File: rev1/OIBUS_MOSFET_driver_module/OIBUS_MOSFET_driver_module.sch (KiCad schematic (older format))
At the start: 149 parts, among them J1 SWD, J10 +, J11 +, J12 +, J13 +, J2 UART, J3 5V - 24V, Molex Ultrafit, J4 +, J5 +, J6 +, J7 +, J8 +, J9 +, T1 DMG6402LVT, T10 DMG6402LVT, T2 DMG6402LVT, T3 DMG6402LVT, T4 DMG6402LVT, T5 DMG6402LVT, T6 DMG6402LVT, T7 DMG6402LVT, T8 DMG6402LVT, T9 DMG6402LVT, U1 TLP291, U10 STM32F303CCTx, U11 TLP291, U12 TLP291, U2 TLP291, U3 TLP291, U4 TLP291, U5 TLP291, U6 TLP291, U7 TLP291, U8 TLP291, U9 TCAN330, Y1 16M

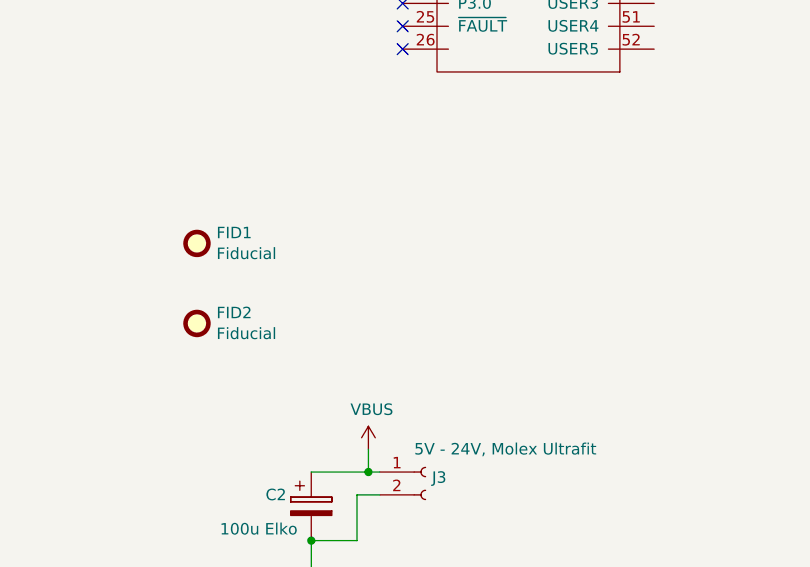
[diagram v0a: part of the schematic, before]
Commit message: disabling bottom solder stencil. uploading to aisler
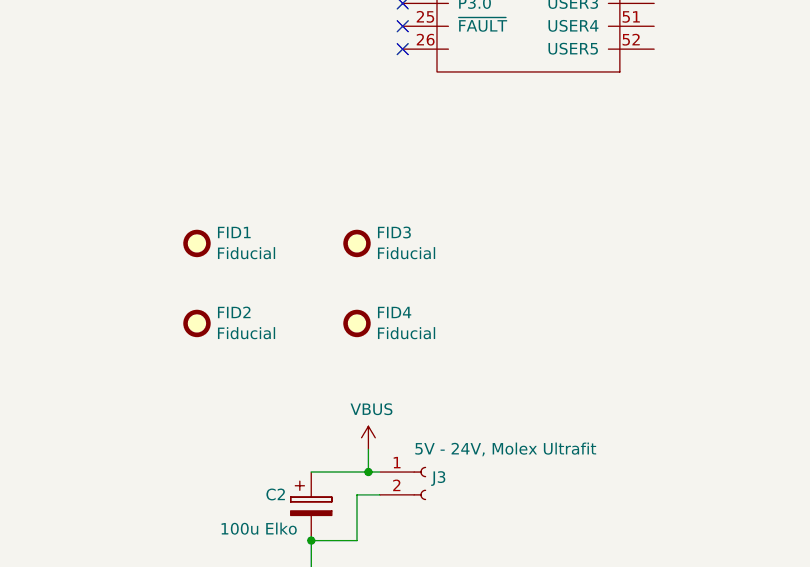
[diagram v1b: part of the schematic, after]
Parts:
- added FID3, FID4: Fiducial, Fiducials:Fiducial_1mm_Dia_2mm_Outer, symbol Mechanical:Fiducial
- FID1, FID2: footprint Fiducial:Fiducial_1mm_Dia_2mm_Outer -> Fiducials:Fiducial_1mm_Dia_2mm_Outer
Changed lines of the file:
@@
 F 0 "FID1" H 9685 9246 50  0000 L CNN
 F 1 "Fiducial" H 9685 9155 50  0000 L CNN
-F 2 "Fiducial:Fiducial_1mm_Dia_2mm_Outer" H 9600 9200 50  0001 C CNN
+F 2 "Fiducials:Fiducial_1mm_Dia_2mm_Outer" H 9600 9200 50  0001 C CNN
 F 3 "~" H 9600 9200 50  0001 C CNN
 	1    9600 9200
@@
 F 0 "FID2" H 9685 9596 50  0000 L CNN
 F 1 "Fiducial" H 9685 9505 50  0000 L CNN
-F 2 "Fiducial:Fiducial_1mm_Dia_2mm_Outer" H 9600 9550 50  0001 C CNN
+F 2 "Fiducials:Fiducial_1mm_Dia_2mm_Outer" H 9600 9550 50  0001 C CNN
 F 3 "~" H 9600 9550 50  0001 C CNN
 	1    9600 9550
@@
 Wire Wire Line
 	11650 7150 11650 7200
+$Comp
+L Mechanical:Fiducial FID4
+U 1 1 5C341F6F
+P 10300 9550
+F 0 "FID4" H 10385 9596 50  0000 L CNN
+F 1 "Fiducial" H 10385 9505 50  0000 L CNN
+F 2 "Fiducials:Fiducial_1mm_Dia_2mm_Outer" H 10300 9550 50  0001 C CNN
+F 3 "~" H 10300 9550 50  0001 C CNN
+	1    10300 9550
+	1    0    0    -1
+$EndComp
+$Comp
+L Mechanical:Fiducial FID3
+U 1 1 5C3420AA
+P 10300 9200
+F 0 "FID3" H 10385 9246 50  0000 L CNN
+F 1 "Fiducial" H 10385 9155 50  0000 L CNN
+F 2 "Fiducials:Fiducial_1mm_Dia_2mm_Outer" H 10300 9200 50  0001 C CNN
+F 3 "~" H 10300 9200 50  0001 C CNN
+	1    10300 9200
+	1    0    0    -1
+$EndComp
 $EndSCHEMATC

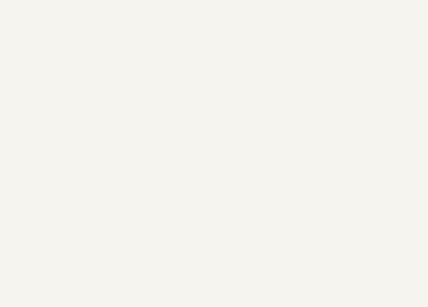
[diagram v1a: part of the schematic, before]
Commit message: silkscreen labels added
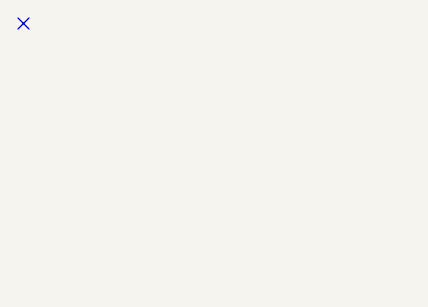
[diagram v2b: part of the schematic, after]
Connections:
- no-connect marks 75 -> 76
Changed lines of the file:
@@
 	1    0    0    -1
 $EndComp
+NoConn ~ -4300 -4150
 $EndSCHEMATC

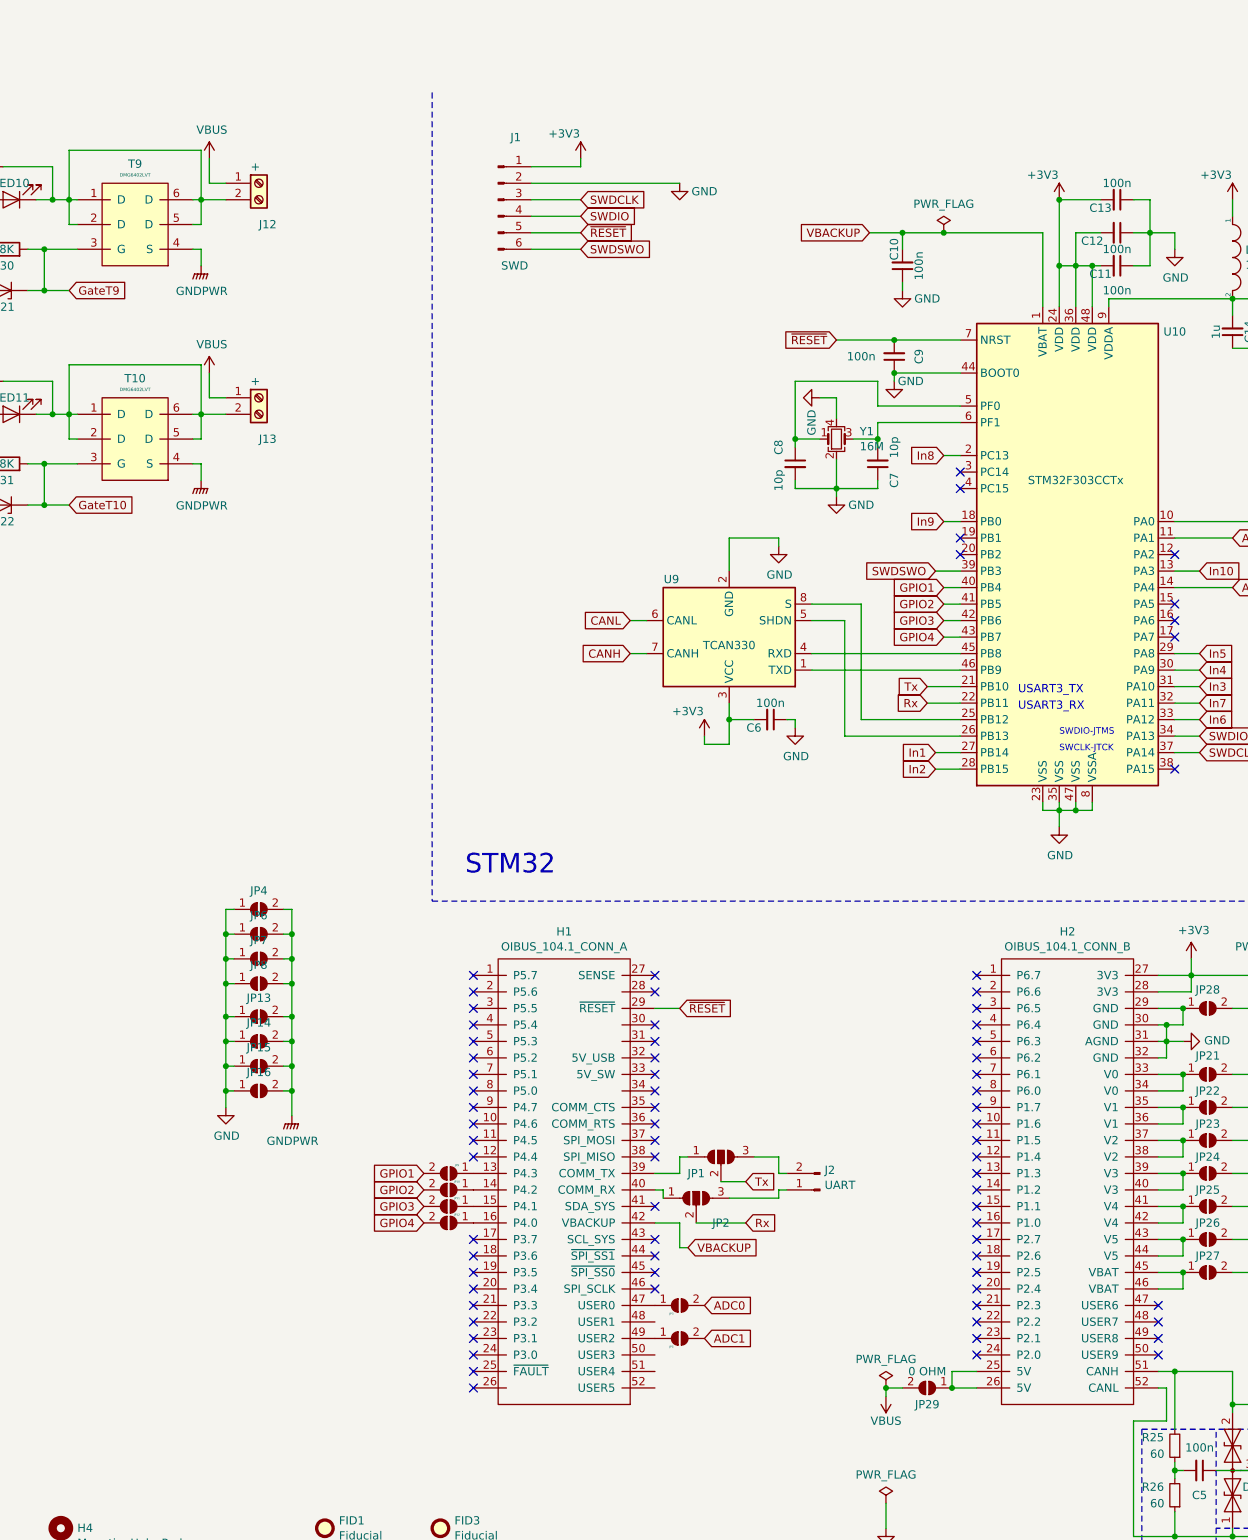
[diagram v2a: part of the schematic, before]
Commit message: fixing zener footprint, rotating leds for side view, added uavcan micro connector
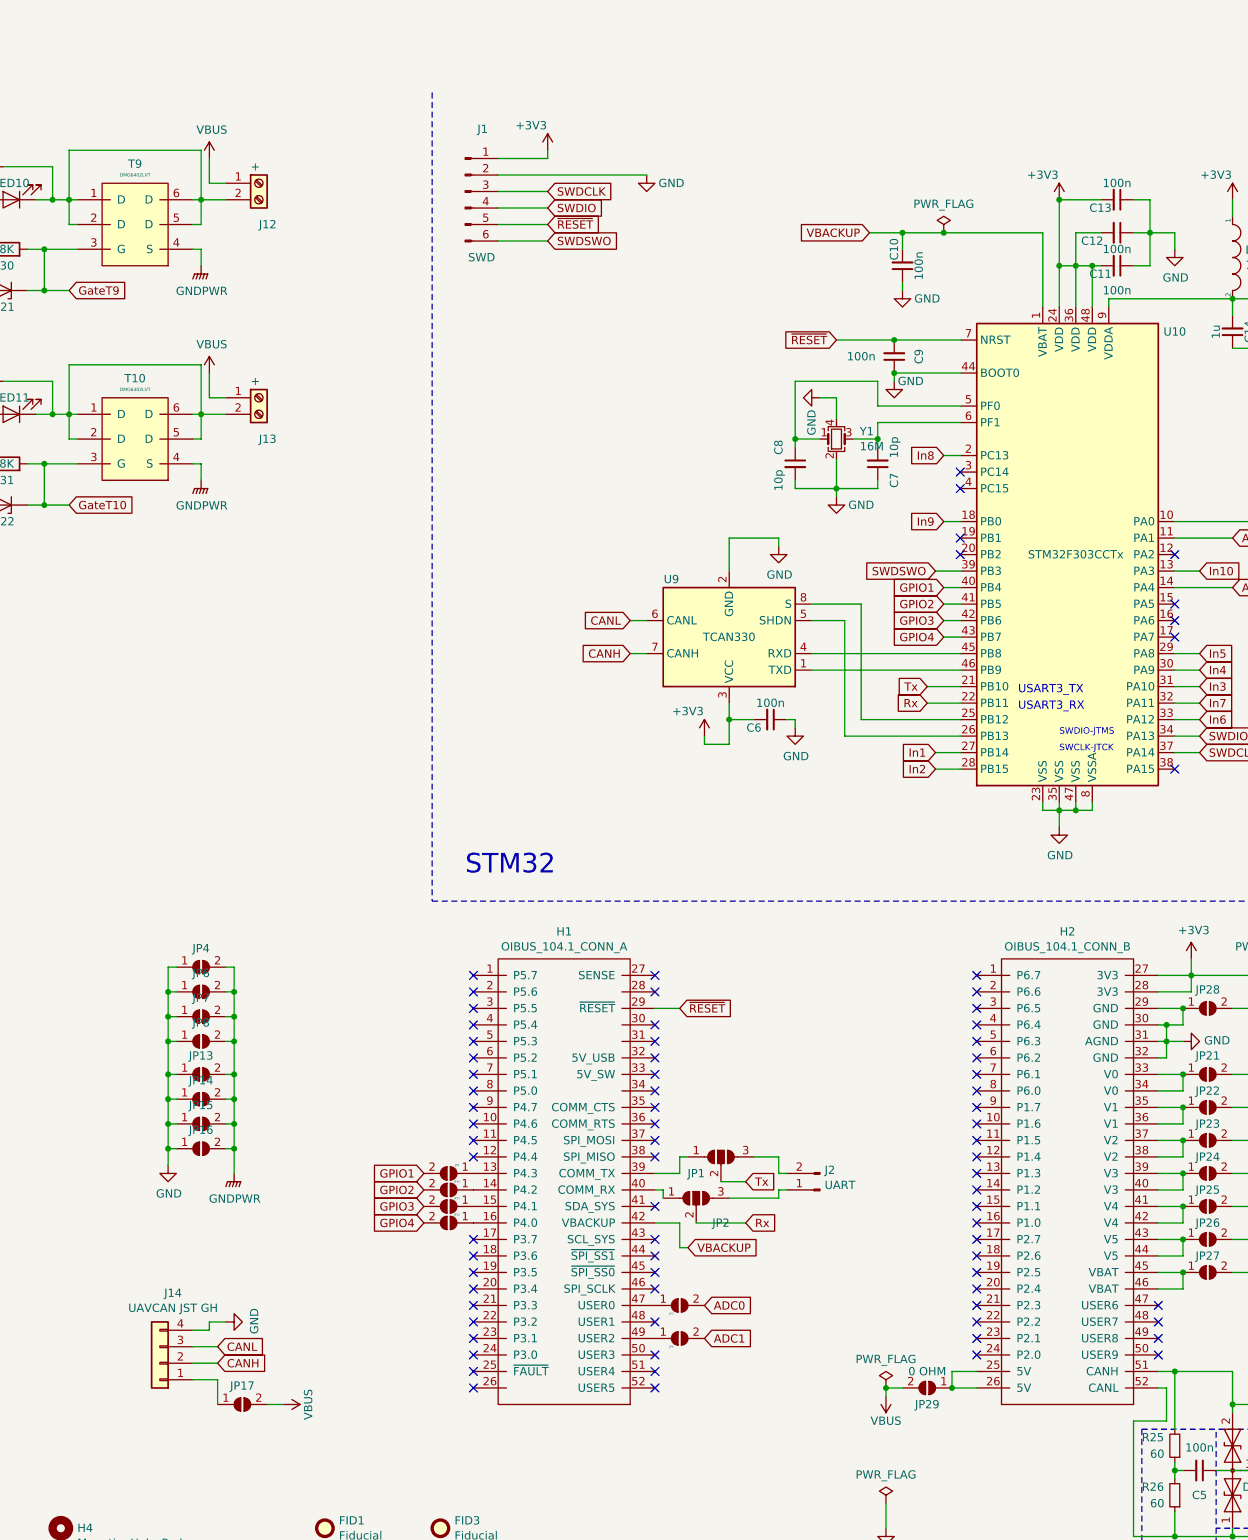
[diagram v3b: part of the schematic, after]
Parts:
- added J14: UAVCAN JST GH, Connectors_JST:JST_GH_SM04B-GHS-TB_04x1.25mm_Angled, symbol Connector_Generic:Conn_01x04
- added JP17: 0 OHM, Resistor_SMD:R_0603_1608Metric, symbol Jumper:SolderJumper_2_Open
- D10, D12, D14, D16, D2, D21, D22, D4, D6, D8: footprint TO_SOT_Packages_SMD:SOT-23 -> Diodes_SMD:D_SOT-23_ANK
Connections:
- net CANH: now also J14.2 (Pin_2)
- net CANL: now also J14.3 (Pin_3)
- net GND: now also J14.4 (Pin_4)
- net VBUS: now also JP17.2 (B)
- new net: J14.1 (Pin_1), JP17.1 (A)
- no-connect marks 76 -> 80
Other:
- moved on the sheet: J1, JP13, JP14, JP15, JP16, JP4, JP6, JP7, JP8

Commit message: created BOM
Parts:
- D18: value D -> 1N5819; symbol Device:D -> Device:D_Schottky
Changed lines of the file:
@@
 Connection ~ 5100 2950
 $Comp
-L Device:D D18
+L Device:D_Schottky D18
 U 1 1 5C083F85
 P 1450 1100
 F 0 "D18" H 1450 1224 50  0000 C CNN
-F 1 "D" H 1450 1225 50  0001 C CNN
+F 1 "1N5819" H 1450 1225 50  0001 C CNN
 F 2 "Diodes_SMD:D_SOD-123" H 1450 1100 50  0001 C CNN
 F 3 "~" H 1450 1100 50  0001 C CNN

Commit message: redesigned for manufacturing, generated PCBA gerber and BOM files
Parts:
- C1, C2: MPN (none) -> EMVA350ADA101MF80G
- C10, C11, C12, C13, C5, C6, C9: MPN (none) -> 885012206095
- C14: MPN (none) -> 885012206076
- C15: MPN (none) -> 885012206089
- C7, C8: MPN (none) -> 885012006051
- D1, D11, D13, D15, D19, D20, D3, D5, D7, D9: MPN (none) -> FM4004-W
- D10, D12, D14, D16, D2, D21, D22, D4, D6, D8: MPN (none) -> BZX84C8V2LT1G
- D17: MPN (none) -> PESD2IVN27-UX
- D18: MPN (none) -> 1N5819HW1-7-F
- H1, H2: MPN (none) -> SSQ-126-22-G-D
- J1: MPN (none) -> 68015-206HLF
- J10, J11, J12, J13, J4, J5, J6, J7, J8, J9: MPN (none) -> CTBP93HE/2
- J14: footprint Connectors_JST:JST_GH_SM04B-GHS-TB_04x1.25mm_Angled -> lib_fp_global:uavcan_connector; symbol Connector_Generic:Conn_01x04 -> uavcan_connector:uavcan; MPN (none) -> SM04B-GHS-TB(LF)(SN)-
- J3: MPN (none) -> 172310-1202
- JP13, JP14, JP15, JP16, JP21, JP22, JP23, JP24, JP25, JP26, JP27, JP28, JP4, JP6, JP7, JP8: value 0 OHM -> 0R; MPN (none) -> RC0603JR-070RL
- JP17, JP29: value 0 OHM -> SolderJumper_2_Open
- L1: MPN (none) -> MLZ2012M100WT000
- LED1, LED10, LED11, LED2, LED3, LED5, LED6, LED7, LED8: value LED -> LED_yellow; MPN (none) -> LTST-S270AKT
- LED4: value LED -> LED_yellow; MPN (none) -> LTST-S270AKT; assembly_note (none) -> side-looking towards PCB edge
- LED9: value LED -> LED_green; MPN (none) -> LTST-S270GKT
- R1, R11, R13, R15, R28, R29, R3, R5, R7, R9: value 4K7 -> 3k6; MPN (none) -> RC0603JR-073K6L
- R10, R12, R14, R16, R2, R30, R31, R4, R6, R8: value 18K -> 18k; MPN (none) -> RC0603JR-0718KL
- R17, R18, R19, R20, R21, R22, R23, R24, R32, R33: value 1K5 -> 1k5; MPN (none) -> RC0603JR-071K5L
- R25, R26: MPN (none) -> RC0603FR-0760R4L
- R27: MPN (none) -> RC0603JR-07330RL
- T1, T10, T2, T3, T4, T5, T6, T7, T8, T9: MPN (none) -> DMG6402LVT-7
- U1, U11, U12, U2, U3, U4, U5, U6, U7, U8: MPN (none) -> TLP291(SE
- U10: MPN (none) -> STM32F303CCT6
- U9: MPN (none) -> TCAN330DCNT
- Y1: MPN (none) -> FA-238 16.0000MA30X-AG0
